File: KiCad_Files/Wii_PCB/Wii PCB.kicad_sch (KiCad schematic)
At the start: 24 parts

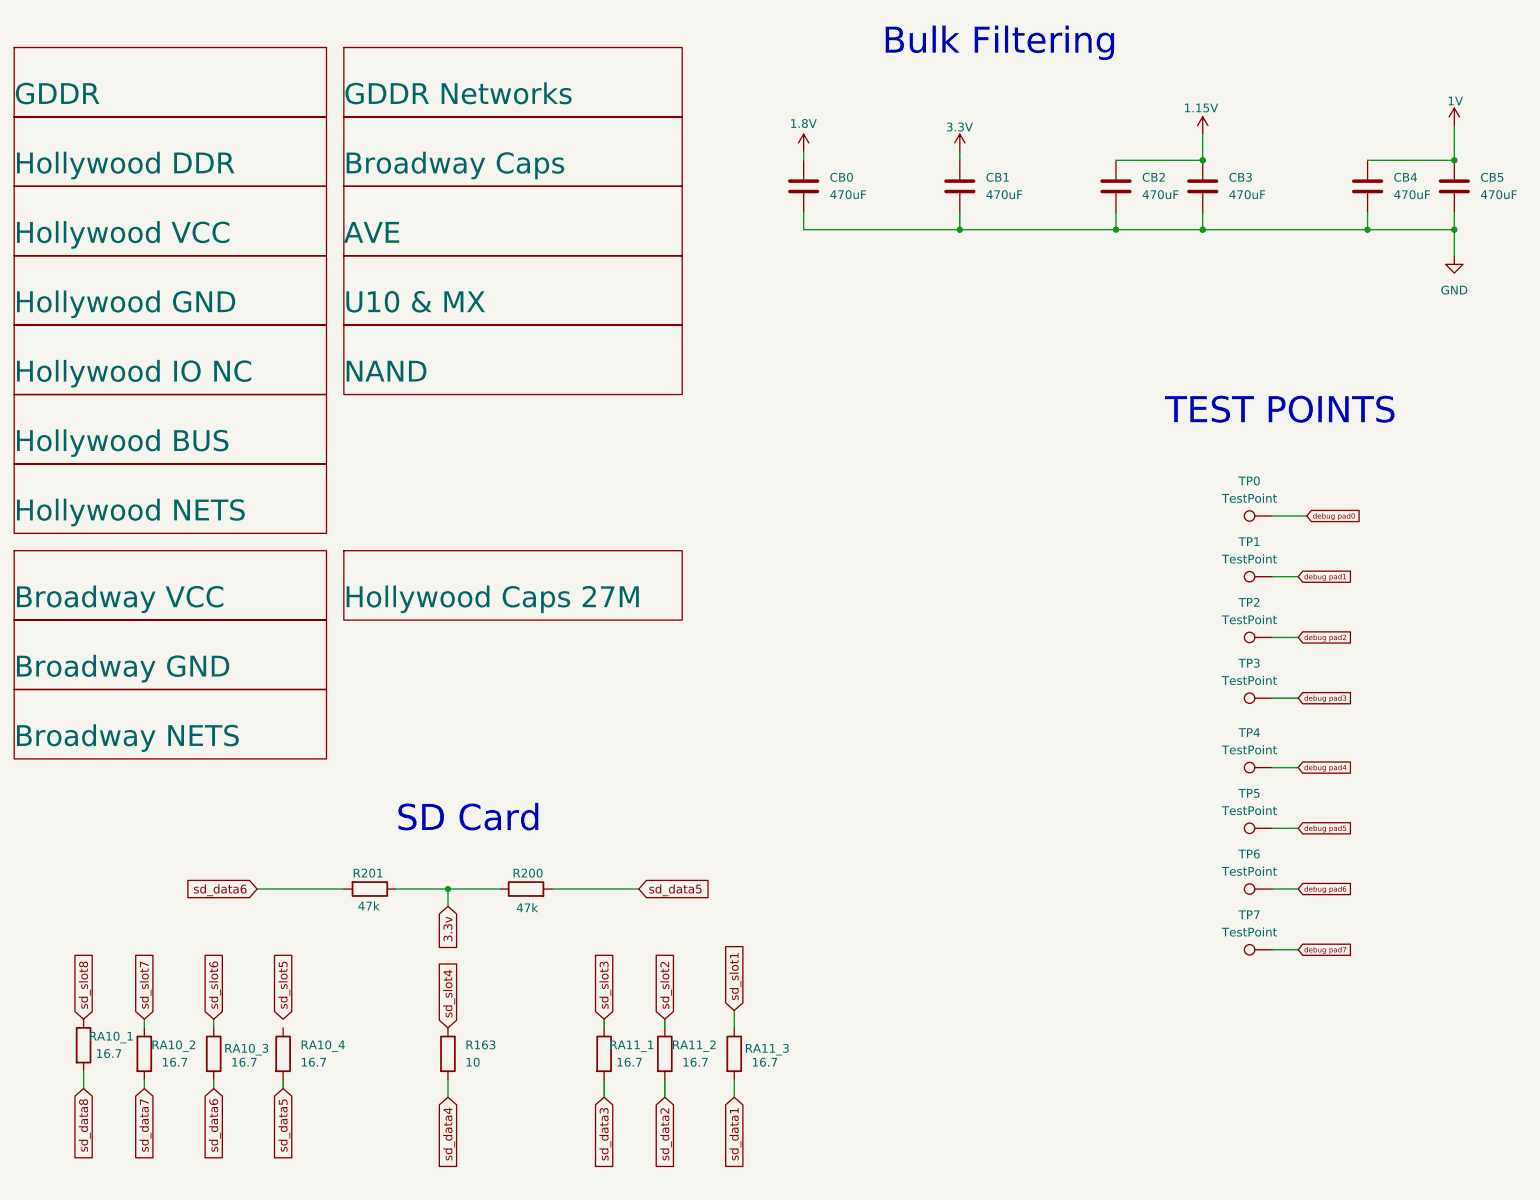
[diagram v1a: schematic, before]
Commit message: Updated RAM & GPU bus to allow custom net rules for measuring intra-track spacing, added pad for reset, removed debug pads, reorganized ram schematic to cluster length matched signals, changed MX chip and U10 symbols, and re-labeled the wifi net interface.
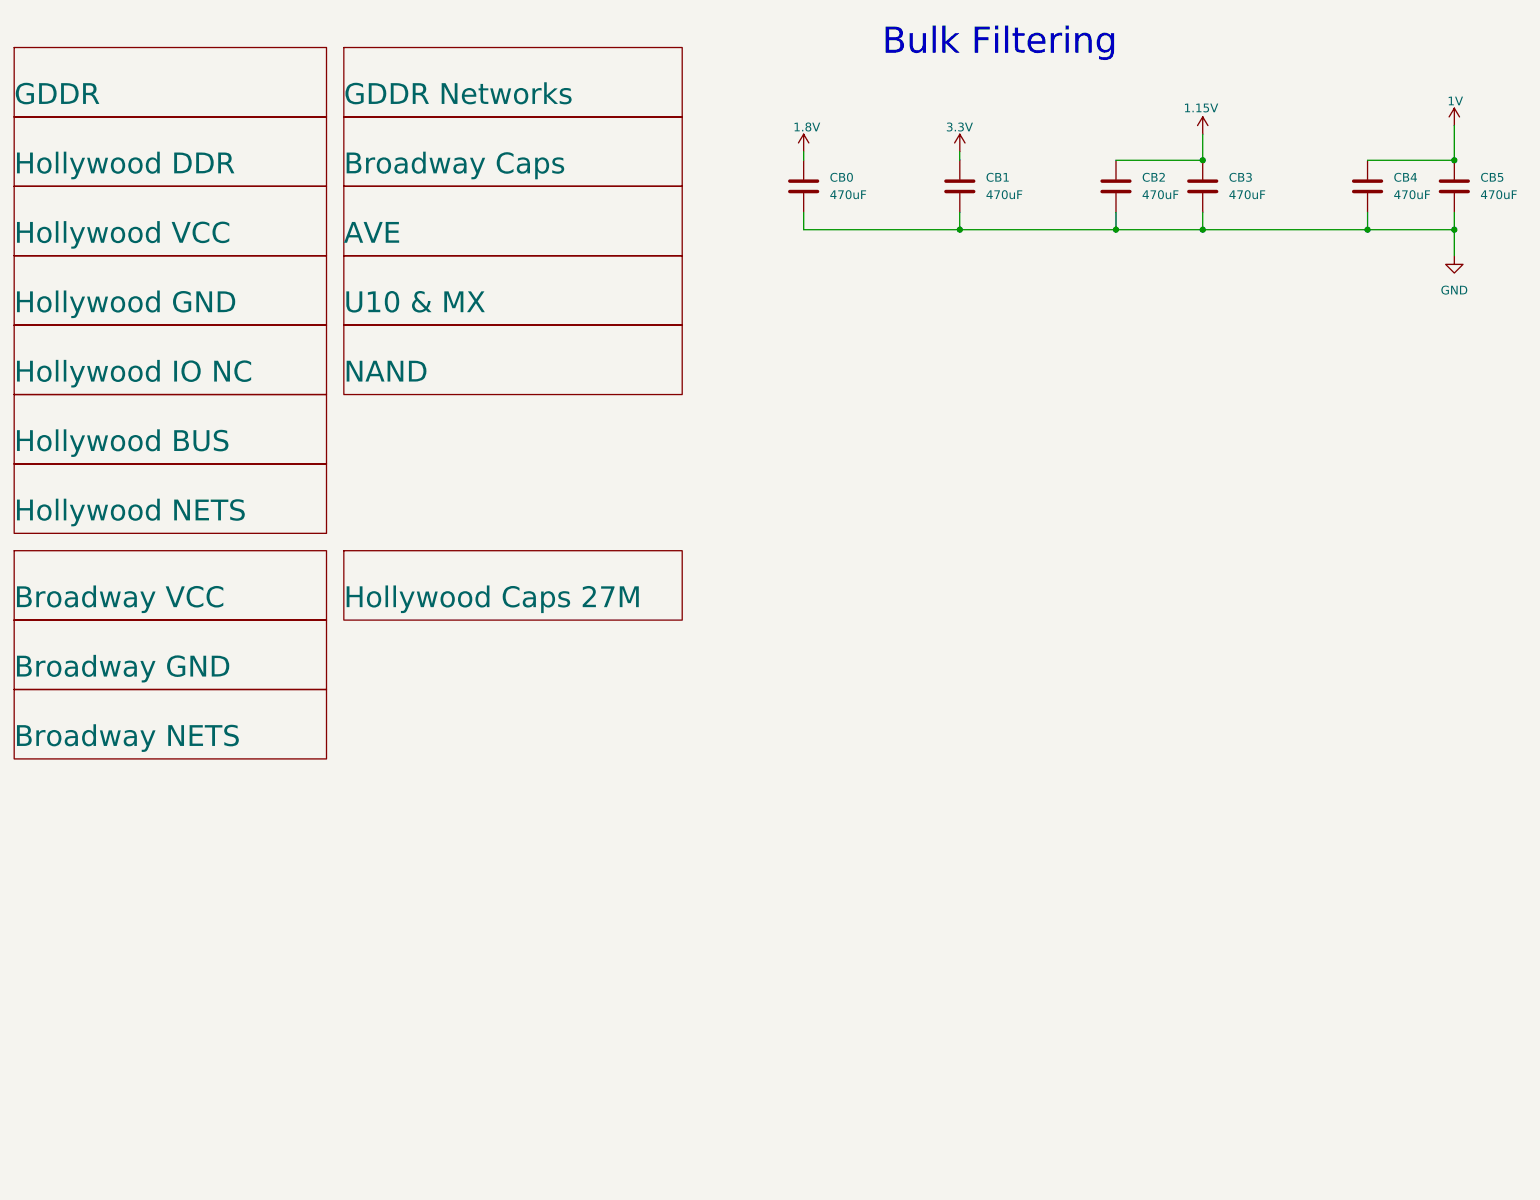
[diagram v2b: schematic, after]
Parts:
- removed R163: 10, Resistor_SMD:R_0402_1005Metric, symbol Device:R
- removed R200, R201: 47k, Resistor_SMD:R_0402_1005Metric, symbol Device:R
- removed RA10_1, RA10_2, RA10_3, RA10_4, RA11_1, RA11_2, RA11_3: 16.7, Resistor_SMD:R_0402_1005Metric, symbol Device:R
- removed TP0, TP1, TP2, TP3, TP4, TP5, TP6, TP7: TestPoint, TestPoint:TestPoint_Pad_D1.0mm, symbol Connector:TestPoint
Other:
- note removed: "SD Card"
- note removed: "TEST POINTS"
